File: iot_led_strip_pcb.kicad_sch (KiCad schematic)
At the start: 38 parts, among them J1 I2C Expansion, J2 Conn_01x03_Socket, J3 GT-USB-7010ASV, J4 Barrel_Jack_Switch_Pin3Ring, J5 TC2050-IDC_Cortex-M, J6 Conn_01x03_Socket_Solderwire, Q1 BSS138, SW1 RESET, SW2 FLASH, U2 ESP32-S2-MINI-1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

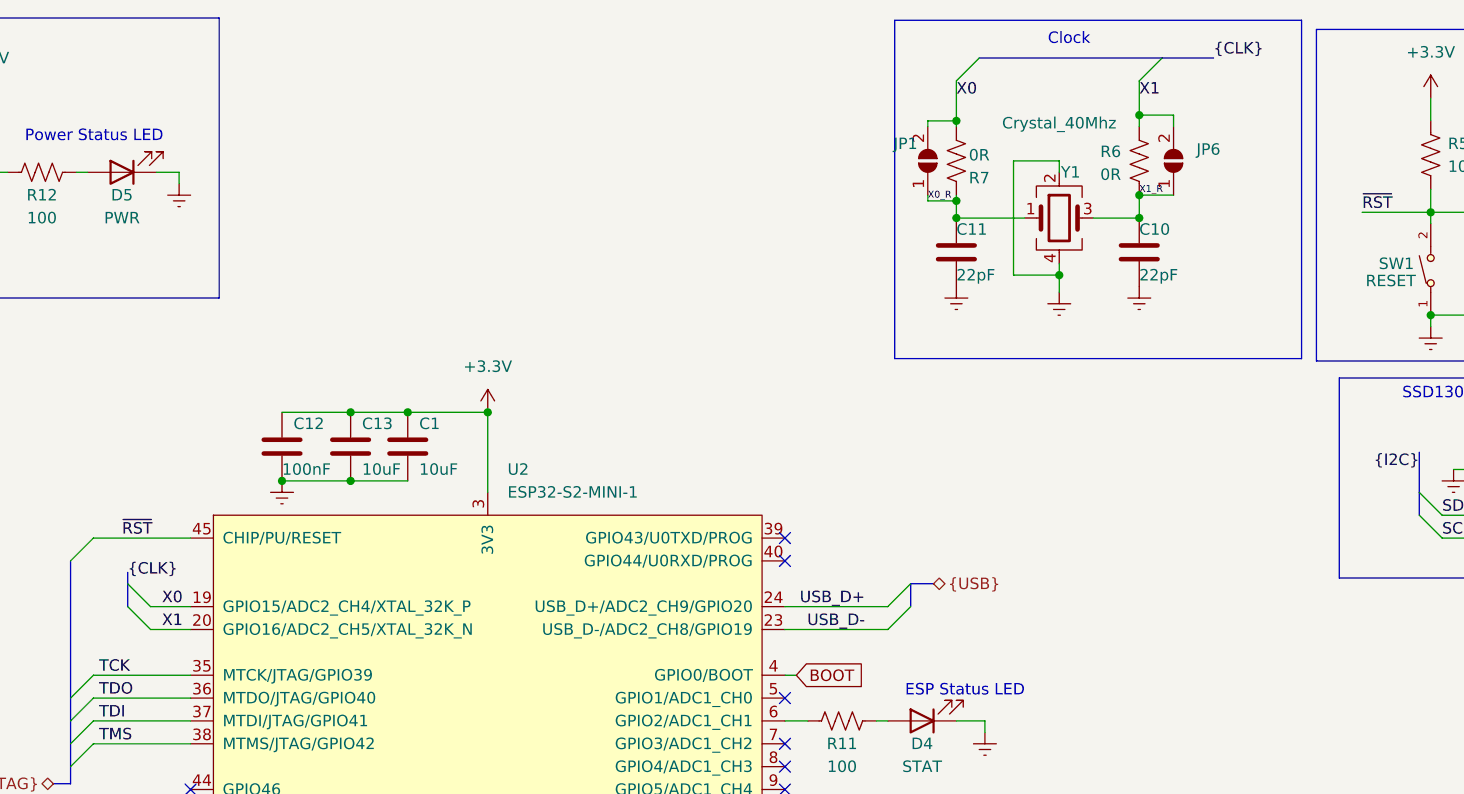
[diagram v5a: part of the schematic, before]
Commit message: PCBA today - field edits on Cs, Rs, removed Rs on Y1
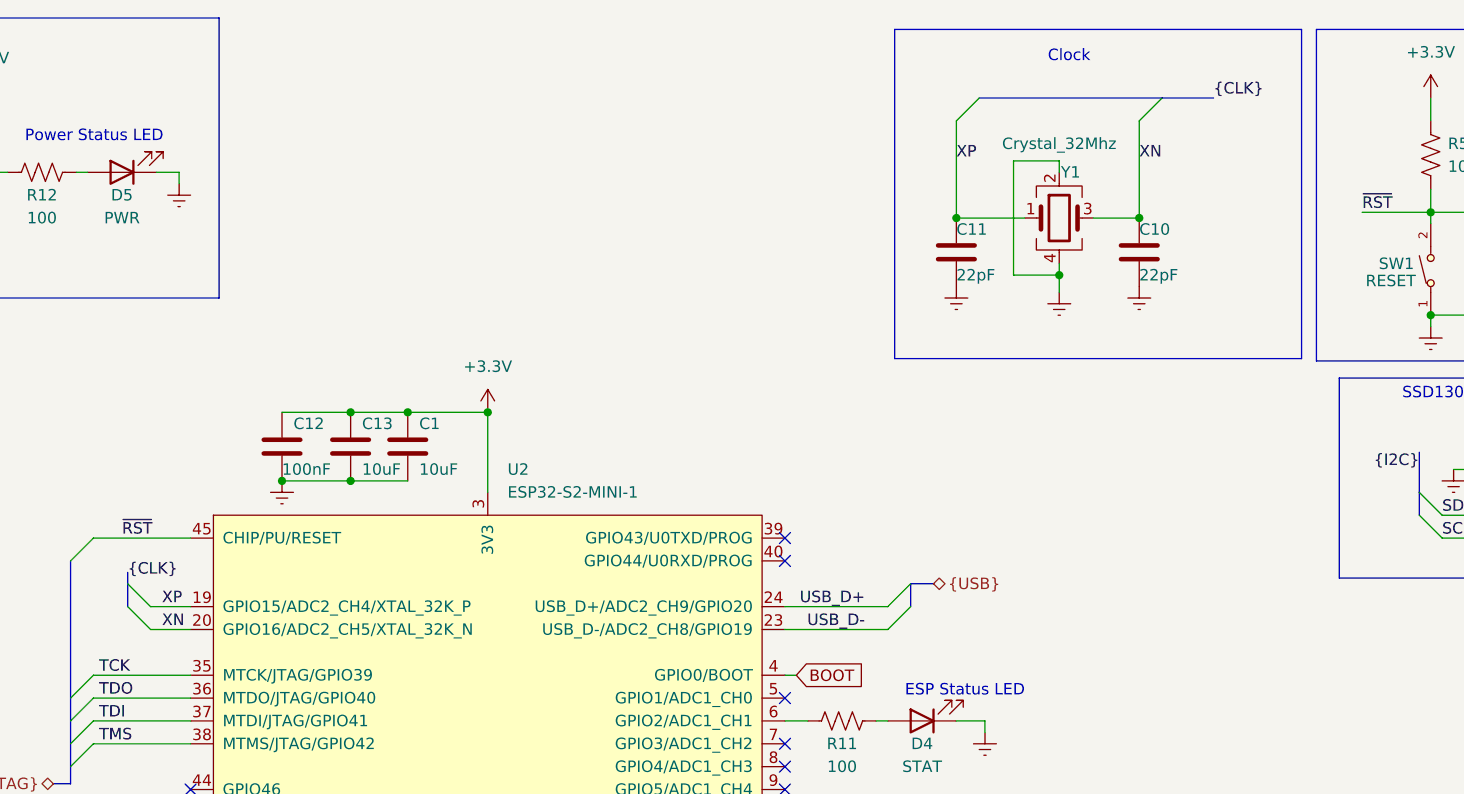
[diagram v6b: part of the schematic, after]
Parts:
- removed JP1, JP6: SolderJumper_2_Open, Jumper:SolderJumper-2_P1.3mm_Open_RoundedPad1.0x1.5mm, symbol Jumper:SolderJumper_2_Open
- removed R6, R7: 0R, Resistor_SMD:R_0805_2012Metric_Pad1.20x1.40mm_HandSolder, symbol Device:R_US
- C8, C9: LCSC C1804 -> (none); Vendor https://www.lcsc.com/product-detail/Multilayer-Ceramic-Capa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 -> (none)
- R10: LCSC C27834 -> (none); Vendor https://www.lcsc.com/product-detail/Chip-Resistor-Surface-M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 -> FILLME
- R3: LCSC C27834 -> (none); Vendor https://www.lcsc.com/product-detail/Chip-Resistor-Surface-M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 -> (none)
- Y1: value Crystal_40Mhz -> Crystal_32Mhz; LCSC C2901712 -> (none); Vendor https://jlcpcb.com/partdetail/3151525-SX3B40000F1210F30/C29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 -> FILLME
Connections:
- net X0_R is gone; now on net XP: C11.1, Y1.1
- net X1_R is gone; now on net XN: C10.1, Y1.3
- net X0 renamed XP
- net X1 renamed XN

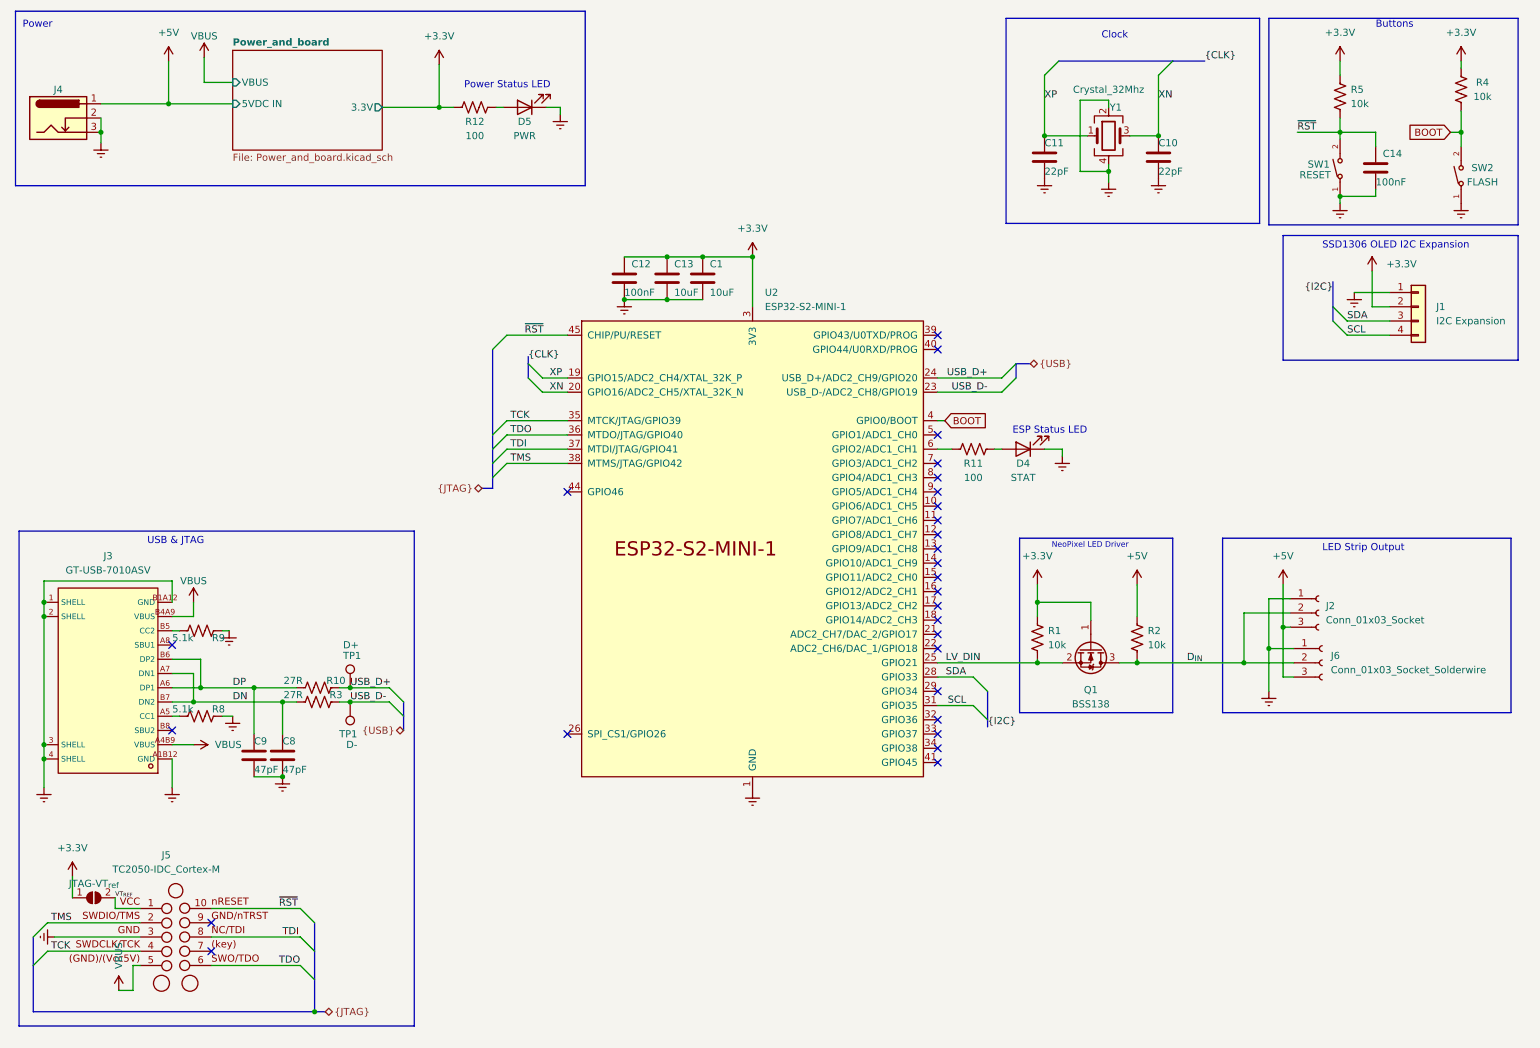
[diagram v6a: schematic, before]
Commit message: modified sch to change over to esp32-s2-solo-2, should be much easier to solder
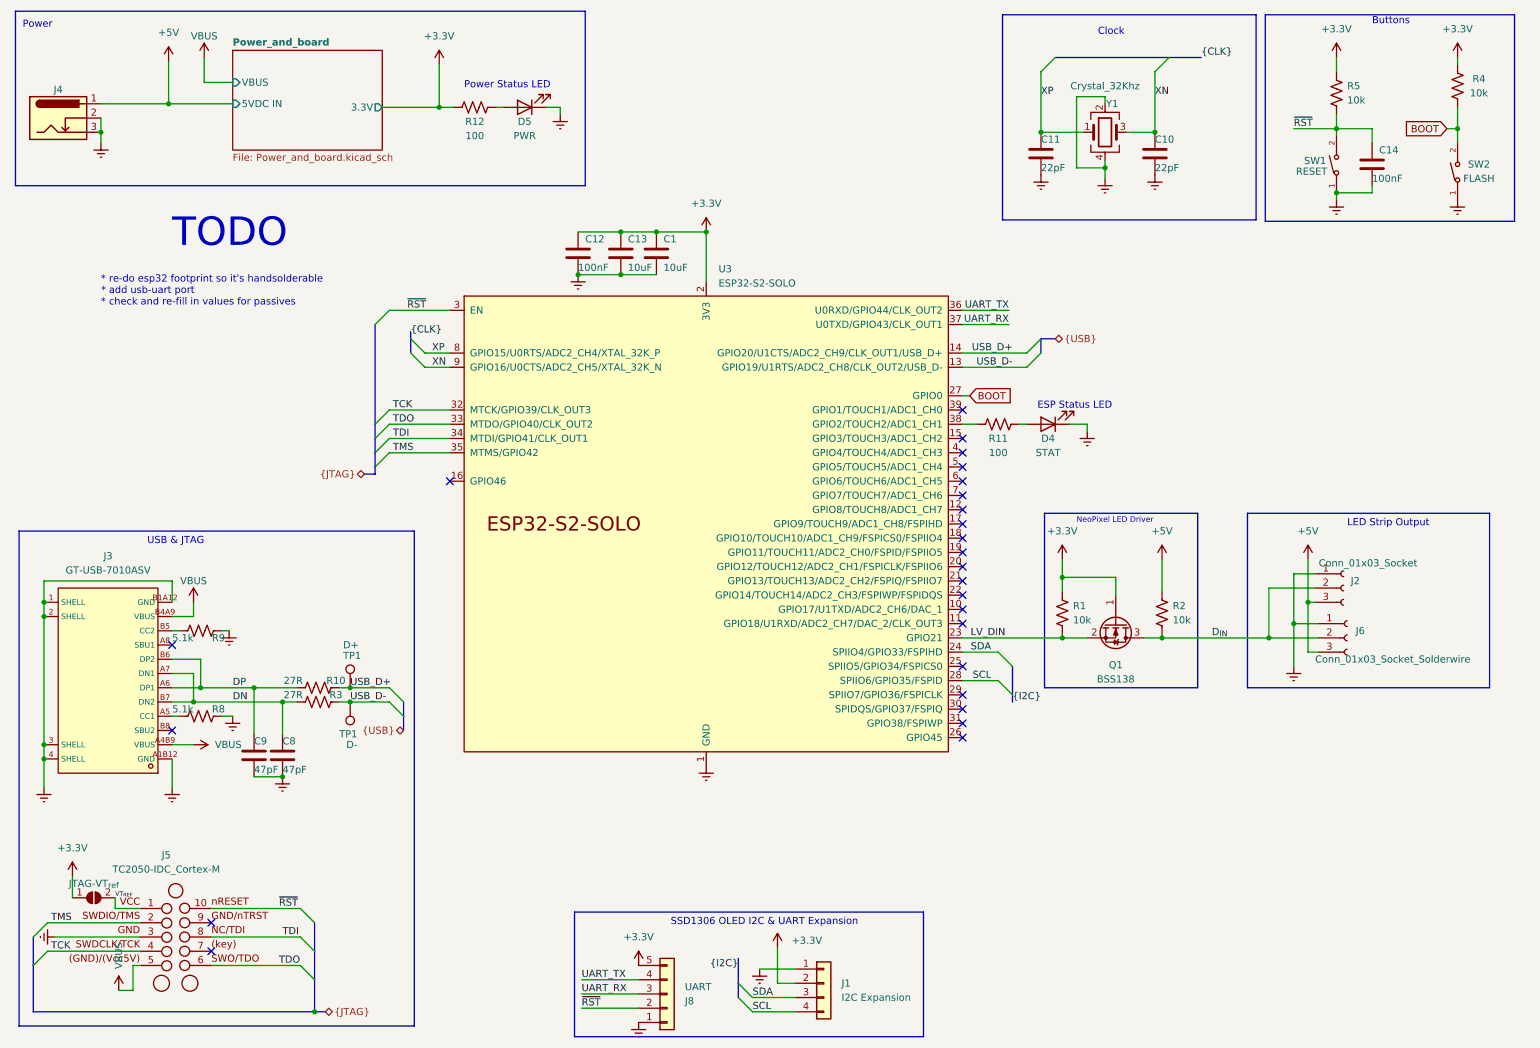
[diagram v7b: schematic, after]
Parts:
- removed U2: ESP32-S2-MINI-1, PCM_Espressif:ESP32-S2-MINI-1, symbol PCM_Espressif:ESP32-S2-MINI-1
- added J8: UART, Connector_PinSocket_2.54mm:PinSocket_1x05_P2.54mm_Vertical, symbol Connector_Generic:Conn_01x05
- added U3: ESP32-S2-SOLO, Espressif:ESP32-S2-SOLO, symbol PCM_Espressif:ESP32-S2-SOLO
- Y1: value Crystal_32Mhz -> Crystal_32Khz
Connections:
- net +3.3V: now also J8.5 (Pin_5), U3.2 (3V3)
- net BOOT: now also U3.27 (GPIO0)
- net Earth: now also J8.1 (Pin_1), U3.1 (GND), U3.40 (GND), U3.41 (GND)
- net LV_DIN: now also U3.23 (GPIO21)
- net SCL: now also U3.28 (SPIIO6/GPIO35/FSPID)
- net SDA: now also U3.24 (SPIIO4/GPIO33/FSPIHD)
- net TCK: now also U3.32 (MTCK/GPIO39/CLK_OUT3)
- net TDI: now also U3.34 (MTDI/GPIO41/CLK_OUT1)
- net TDO: now also U3.33 (MTDO/GPIO40/CLK_OUT2)
- net TMS: now also U3.35 (MTMS/GPIO42)
- net USB_D+: now also U3.14 (GPIO20/U1CTS/ADC2_CH9/CLK_OUT1/USB_D+)
- net USB_D-: now also U3.13 (GPIO19/U1RTS/ADC2_CH8/CLK_OUT2/USB_D-)
- net XN: now also U3.9 (GPIO16/U0CTS/ADC2_CH5/XTAL_32K_N)
- net XP: now also U3.8 (GPIO15/U0RTS/ADC2_CH4/XTAL_32K_P)
- net ~{RST}: now also J8.2 (Pin_2), U3.3 (EN)
- net at R11.2: now also U3.38 (GPIO2/TOUCH2/ADC1_CH1)
- new net UART_RX: J8.3 (Pin_3), U3.37 (U0TXD/GPIO43/CLK_OUT1)
- new net UART_TX: J8.4 (Pin_4), U3.36 (U0RXD/GPIO44/CLK_OUT2)
- no-connect marks 28 -> 25
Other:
- note added: "* re-do esp32 footprint so it's handsolderable * add usb-uart port * check and re-fill in values for passives"
- note added: "SSD1306 OLED I2C & UART Expansion"
- note added: "TODO"
- note removed: "SSD1306 OLED I2C Expansion"
- moved on the sheet: C1, C10, C11, C12, C13, C14, D4, J1, J2, J6, Q1, R1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

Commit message: board redesign around ESP32-S2-SOLO-2
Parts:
- J8: footprint Connector_PinSocket_2.54mm:PinSocket_1x05_P2.54mm_Vertical -> footprint:5 Pin Pad array; now left out of the parts list
- SW1, SW2: footprint Button_Switch_SMD:SW_SPST_TL3342 -> Button_Switch_SMD:SW_SPST_CK_RS282G05A3
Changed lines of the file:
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@@
       (effects (font (size 1.27 1.27)))
     )
-    (property "Footprint" "Button_Switch_SMD:SW_SPST_TL3342" (at 281.305 42.545 0)
+    (property "Footprint" "Button_Switch_SMD:SW_SPST_CK_RS282G05A3" (at 281.305 42.545 0)
       (effects (font (size 1.27 1.27) italic) hide)
     )
@@
   )
   (symbol (lib_id "Connector_Generic:Conn_01x05") (at 130.175 189.23 0) (mirror x) (unit 1)
-    (in_bom yes) (on_board yes) (dnp no)
+    (in_bom no) (on_board yes) (dnp no)
     (property "Reference" "J8" (at 133.35 190.5 0)
       (effects (font (size 1.27 1.27)) (justify left))
@@
       (effects (font (size 1.27 1.27)) (justify left))
     )
-    (property "Footprint" "Connector_PinSocket_2.54mm:PinSocket_1x05_P2.54mm_Vertical" (at 130.175 189.23 0)
+    (property "Footprint" "footprint:5 Pin Pad array" (at 130.175 189.23 0)
       (effects (font (size 1.27 1.27)) hide)
     )
@@
       (effects (font (size 1.27 1.27)))
     )
-    (property "Footprint" "Button_Switch_SMD:SW_SPST_TL3342" (at 259.715 41.275 0)
+    (property "Footprint" "Button_Switch_SMD:SW_SPST_CK_RS282G05A3" (at 259.715 41.275 0)
       (effects (font (size 1.27 1.27) italic) hide)
     )
